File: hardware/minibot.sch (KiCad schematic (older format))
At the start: 30 parts

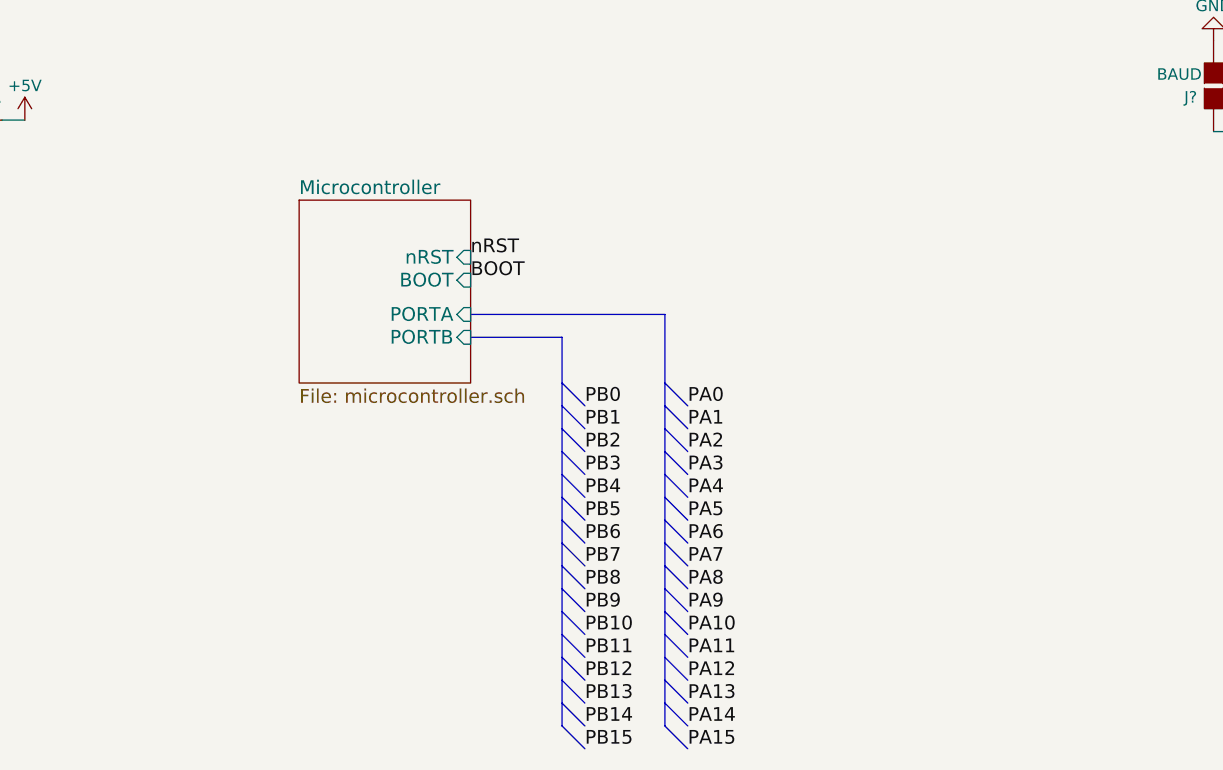
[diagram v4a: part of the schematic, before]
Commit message: Fix the PORT A numbering. Add the ST Link JTAG connector
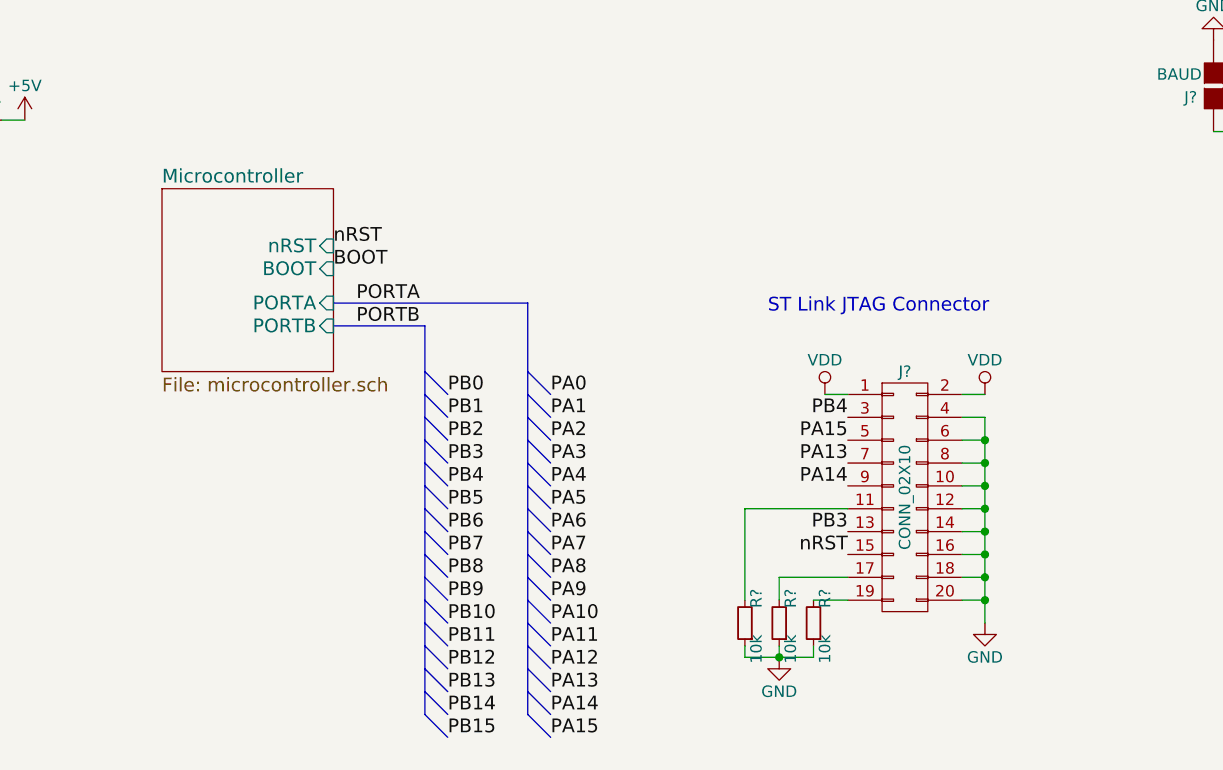
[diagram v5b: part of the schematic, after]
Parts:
- added J?: CONN_02X10, symbol CONN_02X10
- added R? (x3): 10k, symbol R_Small
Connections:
- net GND: now also J?.10 (P10), J?.12 (P12), J?.14 (P14), J?.16 (P16), J?.18 (P18), J?.20 (P20), J?.4 (P4), J?.6 (P6), J?.8 (P8), R?.1, R?.1, R?.1
- net PA13: now also J?.7 (P7)
- net PA14: now also J?.9 (P9)
- net PA15: now also J?.5 (P5)
- net PB3: now also J?.13 (P13)
- net PB4: now also J?.3 (P3)
- net VDD: now also J?.1 (P1), J?.2 (P2)
- net nRST: now also J?.15 (P15)
- new net: J?.11 (P11), R?.2
- new net: J?.17 (P17), R?.2
- new net: J?.19 (P19), R?.2
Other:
- note added: "ST Link JTAG Connector"

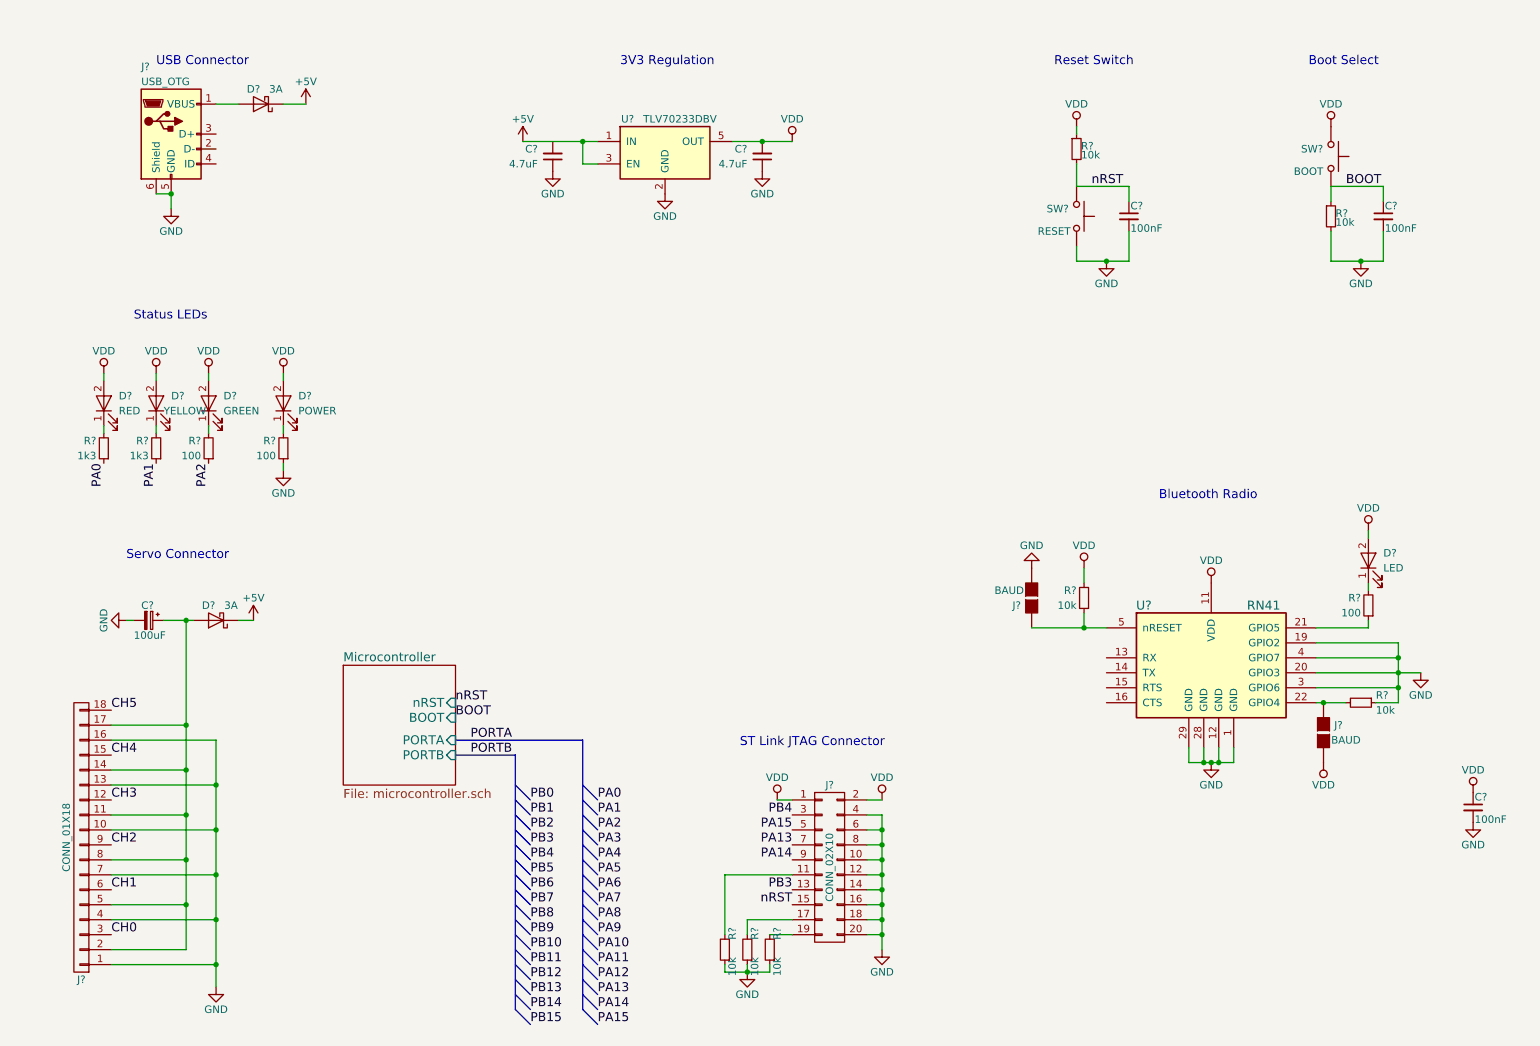
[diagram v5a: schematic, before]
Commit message: Change the JTAG connector to an SWD connector. Also start connecting the MCU pins in a clear and visible manner
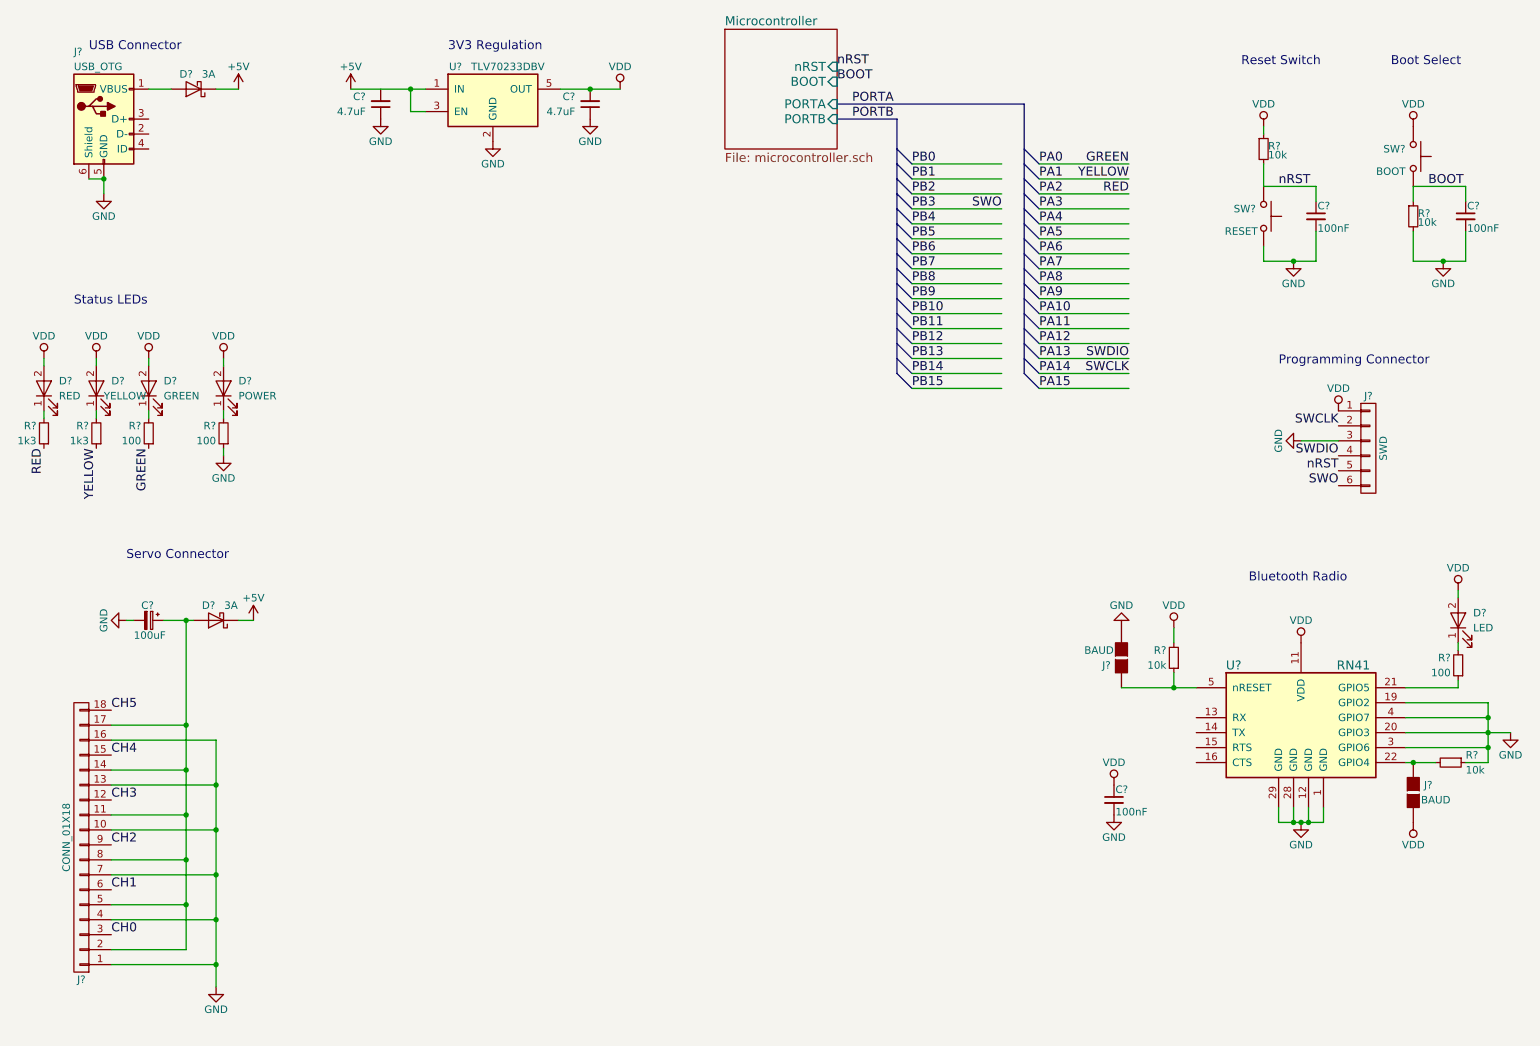
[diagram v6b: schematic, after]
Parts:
- removed J?: CONN_02X10, symbol CONN_02X10
- removed R? (x3): 10k, symbol R_Small
- added J?: SWD, symbol CONN_01X06
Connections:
- net labels added: GREEN, RED, SWCLK, SWDIO, SWO, YELLOW
- wire segments 88 -> 100
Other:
- note added: "Programming Connector"
- note removed: "ST Link JTAG Connector"
- moved on the sheet: C?, D?, J?, R?, SW?, U?

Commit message: Map the servo channels. Wire up the BT USART. Add an IMU and an I2C bus. Update the schematic PDF.
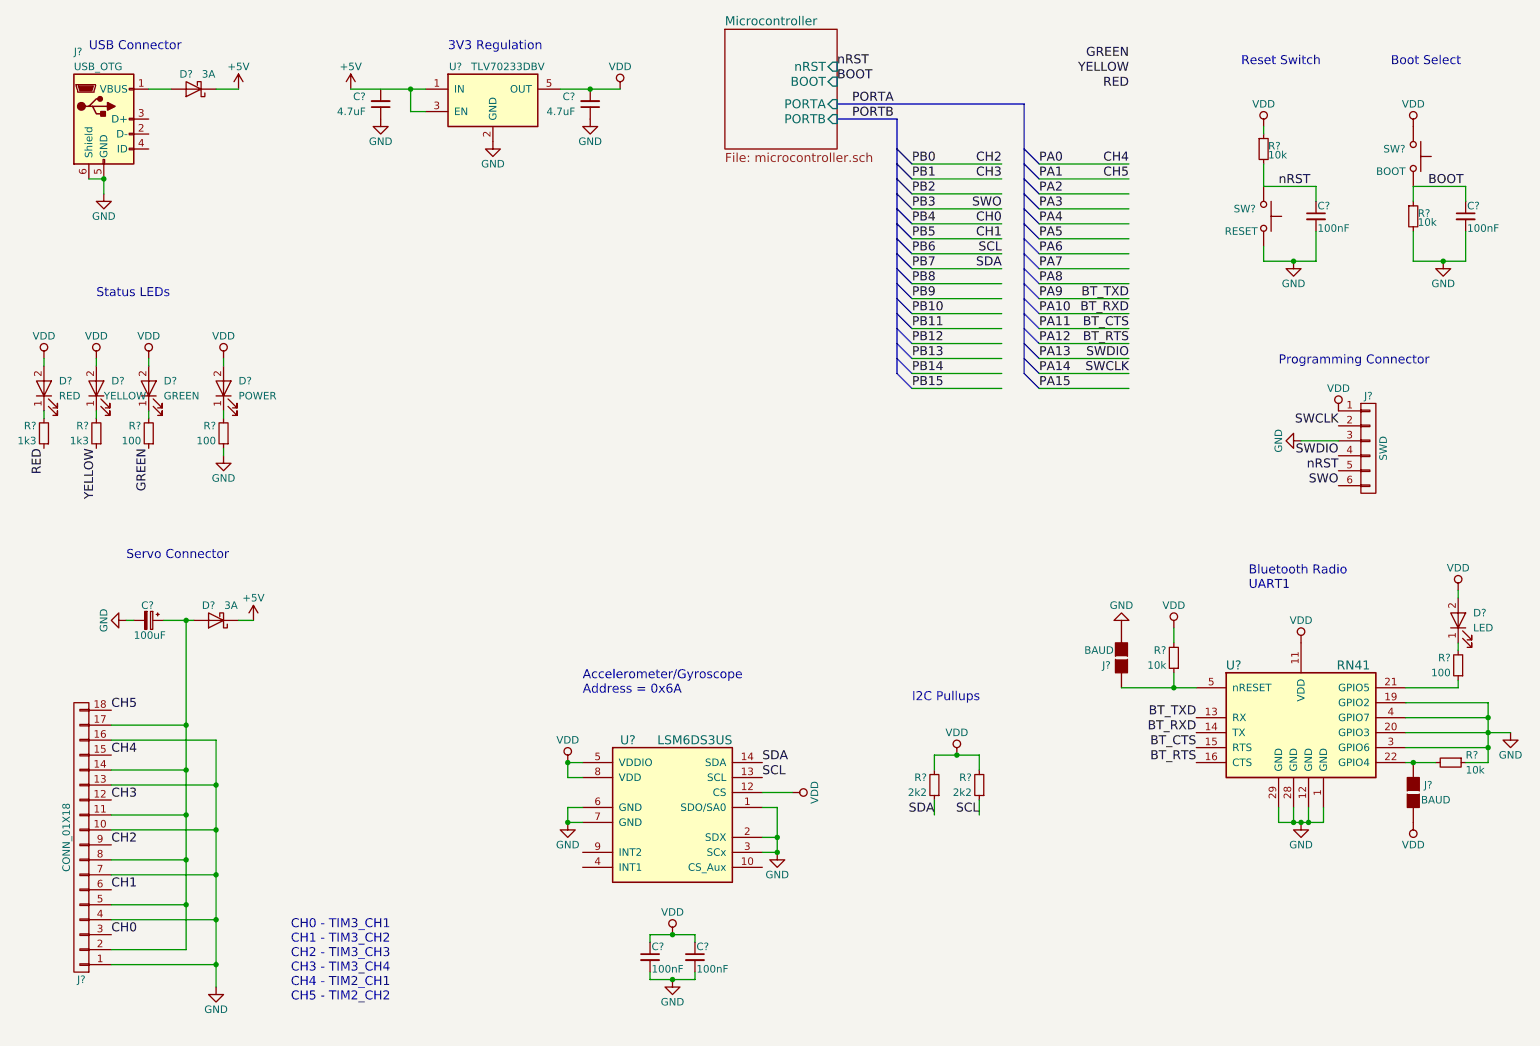
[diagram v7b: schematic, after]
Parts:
- added C?: 100nF, symbol C_Small
- added R? (x2): 2k2, symbol R_Small
- added U?: LSM6DS3US, symbol LSM6DS3US
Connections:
- net labels added: BT_CTS, BT_RTS, BT_RXD, BT_TXD, SCL, SDA
- wire segments 100 -> 122
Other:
- note added: "Accelerometer/Gyroscope\nAddress = 0x6A\n"
- note added: "Bluetooth Radio\nUART1\n"
- note added: "CH0 - TIM3_CH1\nCH1 - TIM3_CH2\nCH2 - TIM3_CH3\nCH3 - TIM3_CH4\nCH4 - TIM2_CH1\nCH5 - TIM2_CH2"
- note added: "I2C Pullups\n"
- note removed: "Bluetooth Radio\n"
- moved on the sheet: C?

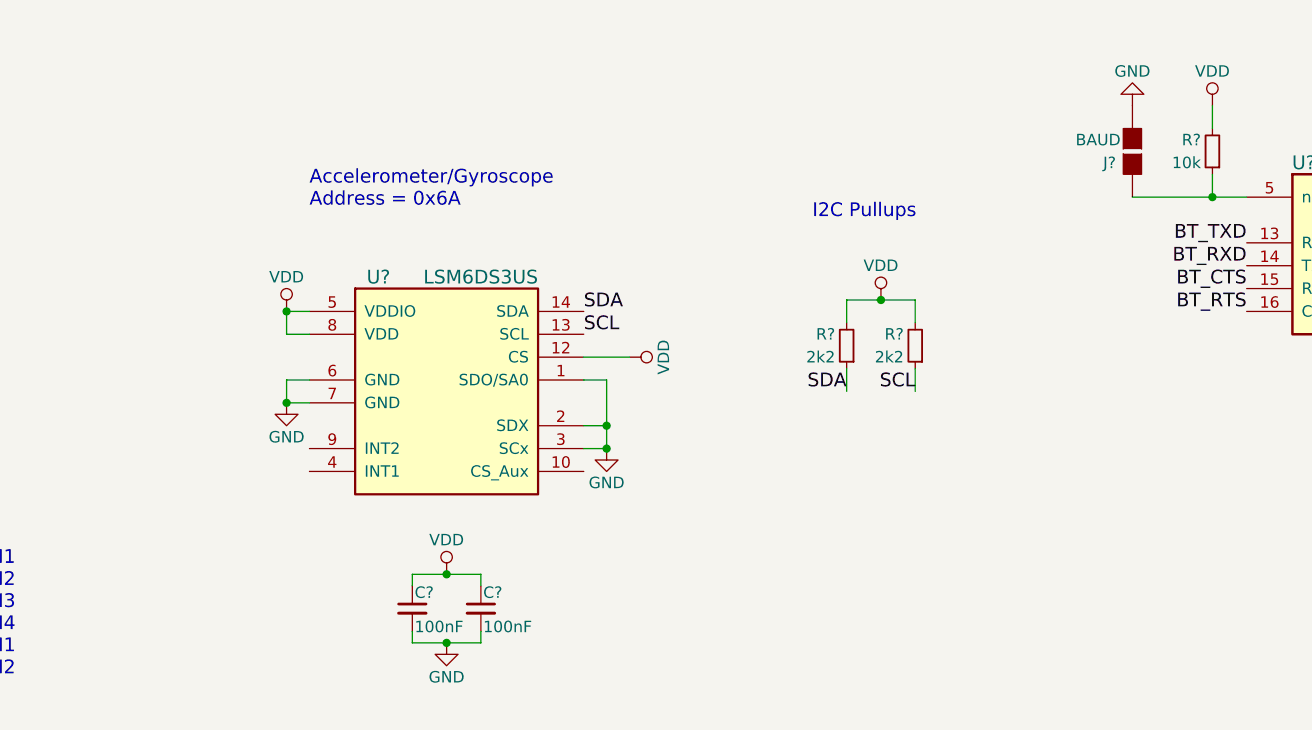
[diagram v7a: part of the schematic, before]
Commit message: Add missing decoupling capacitor to the RN41
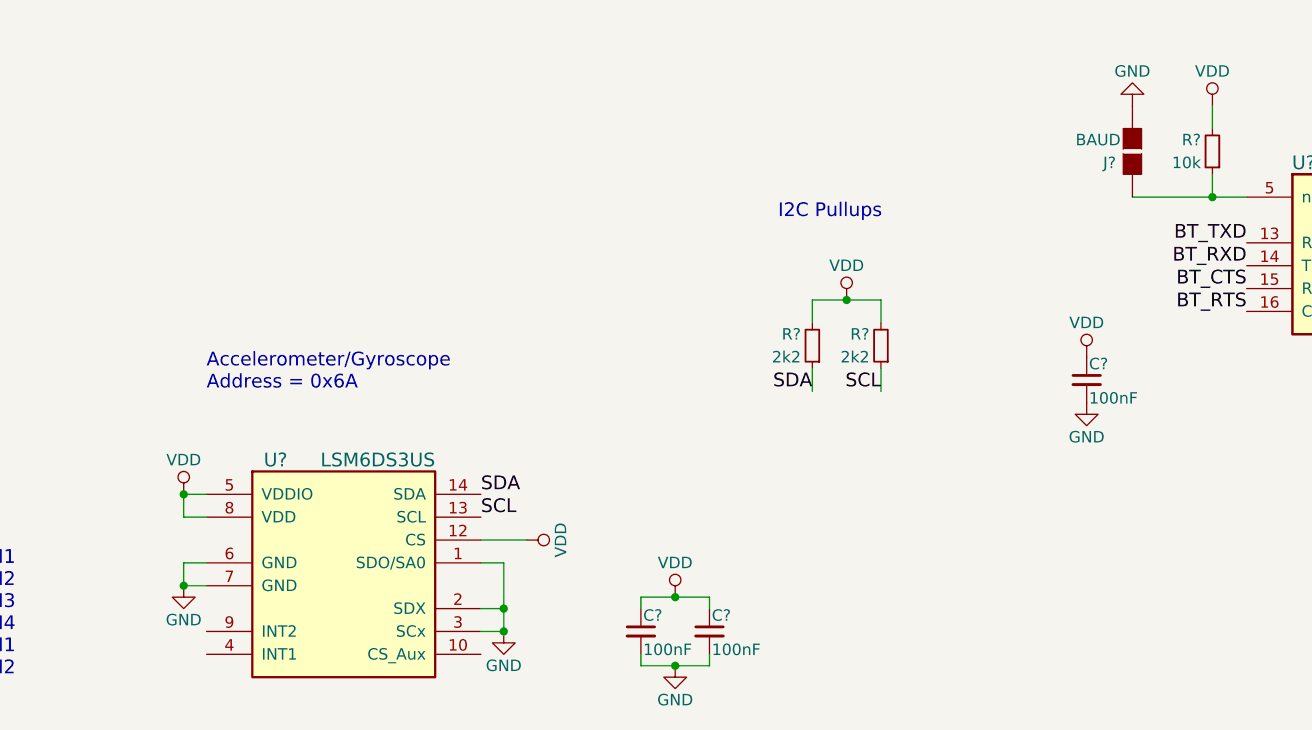
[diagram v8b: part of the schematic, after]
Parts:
- added C?: 100nF, symbol C_Small
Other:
- moved on the sheet: C?, R?, U?
